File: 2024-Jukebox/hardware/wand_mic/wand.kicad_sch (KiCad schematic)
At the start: 51 parts, among them J1 USB_C_Receptacle_USB2.0, J2 Conn_01x05, J3 Conn_01x07, J5 Conn_01x04, J6 Conn_01x01, J7 Conn_01x04, J8 Conn_01x07, Q1 MUN5214DW1T1G, Q2 BSS138, Q3 CJ3139K, Q5 BSS138, SW1 SW_SPDT, U1 CP2104, U2 ESP32-PICO-D4, U3 ICM-20948, U4 TP4065-4.2V, U5 NCP167BMX330TBG, U6 LY68L6400SLIT, U7 MIC5225-1.8

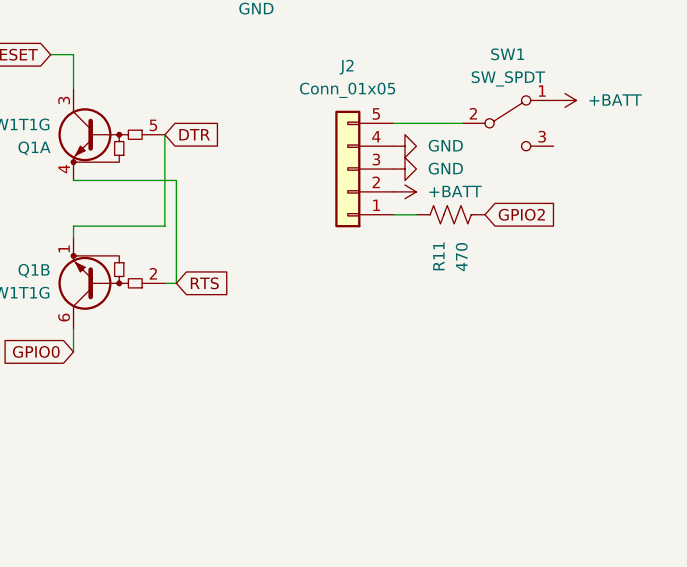
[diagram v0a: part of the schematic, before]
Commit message: Added power selection jumper for LED
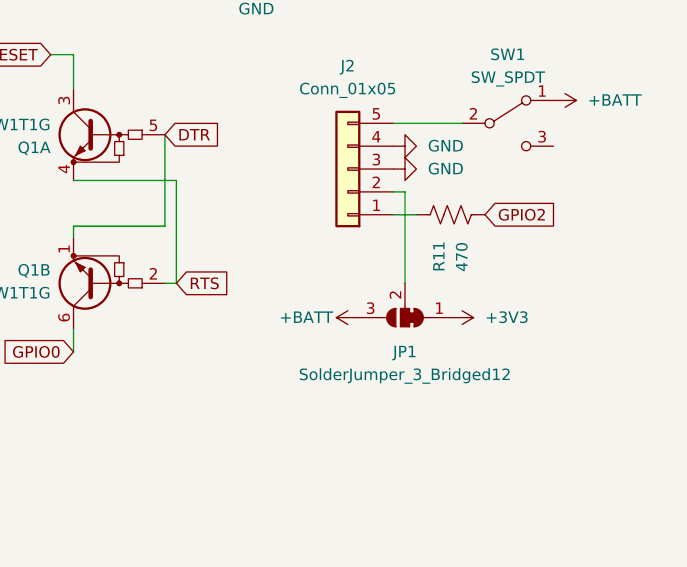
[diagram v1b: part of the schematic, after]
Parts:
- added JP1: SolderJumper_3_Bridged12, Jumper:SolderJumper-3_P1.3mm_Bridged12_RoundedPad1.0x1.5mm, symbol Jumper:SolderJumper_3_Bridged12
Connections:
- net +3V3: now also JP1.1 (A)
- net +BATT: now also JP1.3 (B); no longer J2.2 (Pin_2)
- new net: J2.2 (Pin_2), JP1.2 (C)
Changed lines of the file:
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@@
+    (stroke (width 0) (type default))
+  )
+  (wire (pts (xy 250.19 140.97) (xy 248.92 140.97))
     (stroke (width 0) (type default))
   )
@@
   )
   (wire (pts (xy 139.7 180.34) (xy 152.4 180.34))
+    (stroke (width 0) (type default))
+  )
+  (wire (pts (xy 250.19 151.13) (xy 250.19 140.97))
     (stroke (width 0) (type default))
   )
@@
     )
   )
-  (symbol (lib_id "power:+BATT") (at 248.92 140.97 270) (unit 1)
-    (in_bom yes) (on_board yes) (dnp no) (fields_autoplaced)
-    (property "Reference" "#PWR022" (at 245.11 140.97 0)
-      (effects (font (size 1.27 1.27)) hide)
-    )
-    (property "Value" "+BATT" (at 252.73 140.97 90)
-      (effects (font (size 1.27 1.27)) (justify left))
-    )
-    (property "Footprint" "" (at 248.92 140.97 0)
-      (effects (font (size 1.27 1.27)) hide)
-    )
-    (property "Datasheet" "" (at 248.92 140.97 0)
+  (symbol (lib_id "power:+BATT") (at 245.11 154.94 90) (unit 1)
+    (in_bom yes) (on_board yes) (dnp no)
+    (property "Reference" "#PWR022" (at 248.92 154.94 0)
+      (effects (font (size 1.27 1.27)) hide)
+    )
+    (property "Value" "+BATT" (at 236.22 154.94 90)
+      (effects (font (size 1.27 1.27)) (justify right))
+    )
+    (property "Footprint" "" (at 245.11 154.94 0)
+      (effects (font (size 1.27 1.27)) hide)
+    )
+    (property "Datasheet" "" (at 245.11 154.94 0)
       (effects (font (size 1.27 1.27)) hide)
     )
@@
         (path "/57fbe485-87aa-4709-9ba0-ed0723b6c939"
           (reference "R10") (unit 1)
+        )
+      )
+    )
+  )
+  (symbol (lib_id "power:+3V3") (at 255.27 154.94 270) (unit 1)
+    (in_bom yes) (on_board yes) (dnp no) (fields_autoplaced)
+    (property "Reference" "#PWR010" (at 251.46 154.94 0)
+      (effects (font (size 1.27 1.27)) hide)
+    )
+    (property "Value" "+3V3" (at 259.08 154.94 90)
+      (effects (font (size 1.27 1.27)) (justify left))
+    )
+    (property "Footprint" "" (at 255.27 154.94 0)
+      (effects (font (size 1.27 1.27)) hide)
+    )
+    (property "Datasheet" "" (at 255.27 154.94 0)
+      (effects (font (size 1.27 1.27)) hide)
+    )
+    (pin "1")
+    (instances
+      (project "wand"
+        (path "/57fbe485-87aa-4709-9ba0-ed0723b6c939"
+          (reference "#PWR010") (unit 1)
         )
       )
@@
         )
       )
+    )
+  )
+  (symbol (lib_id "Jumper:SolderJumper_3_Bridged12") (at 250.19 154.94 180) (unit 1)
+    (in_bom yes) (on_board yes) (dnp no) (fields_autoplaced)
+    (property "Reference" "JP1" (at 250.19 158.75 0)
+      (effects (font (size 1.27 1.27)))
+    )
+    (property "Value" "SolderJumper_3_Bridged12" (at 250.19 161.29 0)
+      (effects (font (size 1.27 1.27)))
+    )
+    (property "Footprint" "Jumper:SolderJumper-3_P1.3mm_Bridged12_RoundedPad1.0x1.5mm" (at 250.19 154.94 0)
+      (effects (font (size 1.27 1.27)) hide)
+    )
+    (property "Datasheet" "~" (at 250.19 154.94 0)
+      (effects (font (size 1.27 1.27)) hide)
+    )
+    (pin "2")
+    (pin "1")
+    (pin "3")
+    (instances
+      (project "wand"
+        (path "/57fbe485-87aa-4709-9ba0-ed0723b6c939"
+          (reference "JP1") (unit 1)
+        )
+      )
